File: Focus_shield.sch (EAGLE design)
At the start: 61 parts, among them U1 ARDUINO_SHIELDNOHOLES

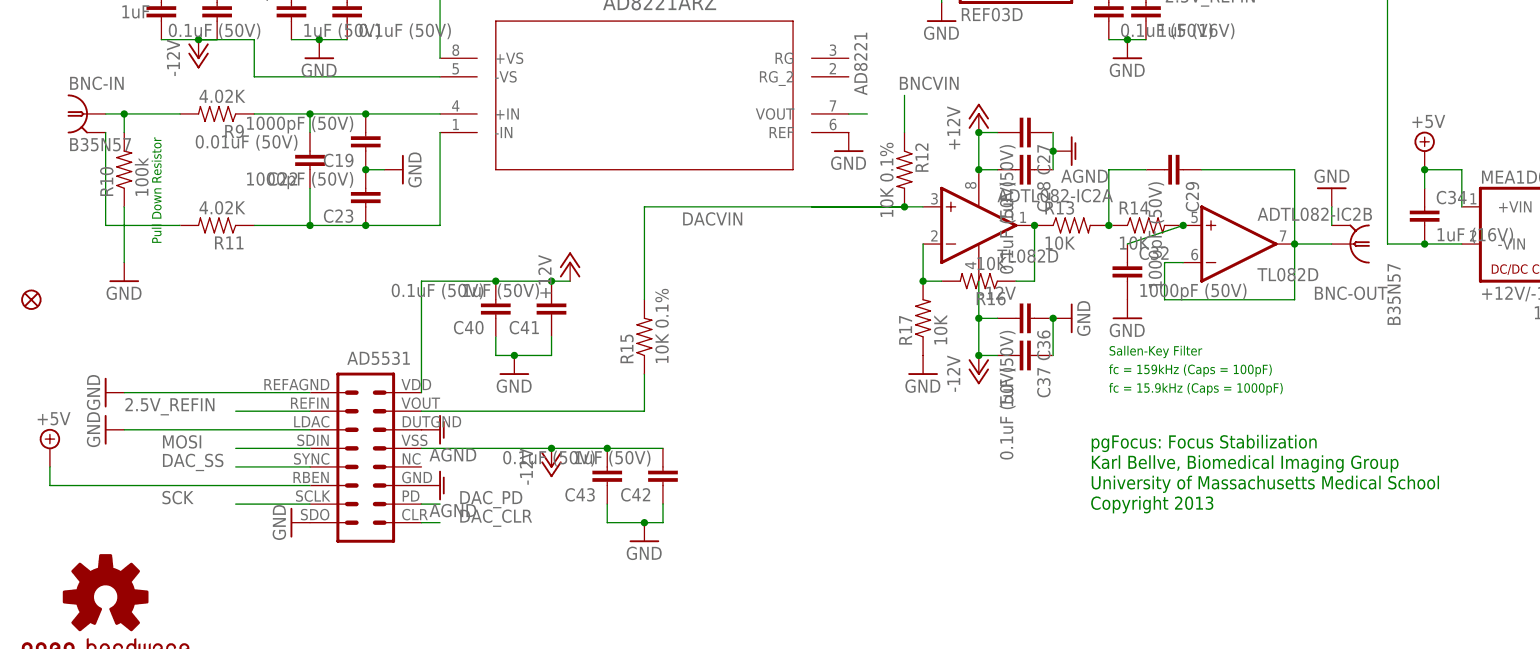
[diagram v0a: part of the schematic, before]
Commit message: switch type of BNC users, and added a link to BOM spreadsheet
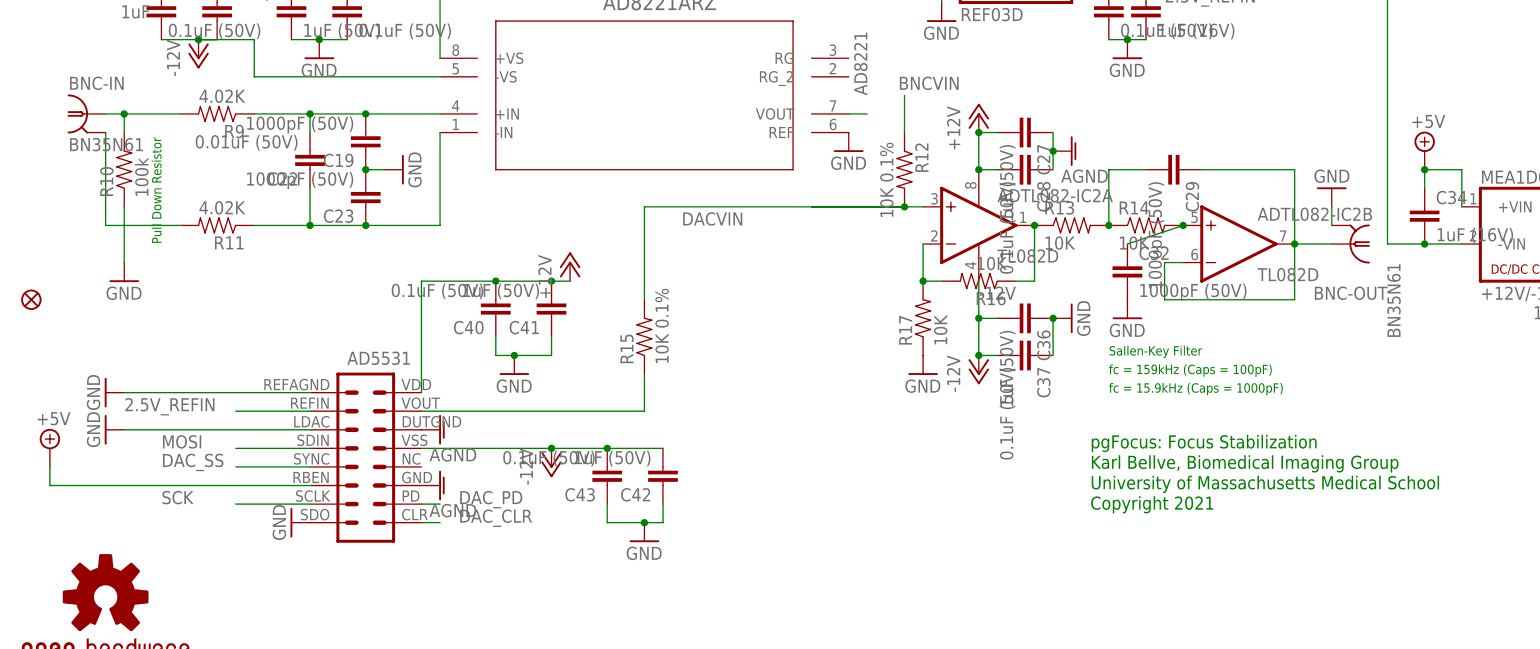
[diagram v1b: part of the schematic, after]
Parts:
- BNC-IN, BNC-OUT: value B35N57 -> BN35N61; device con-coax:B35N57 -> con-coax:BN35N61
- renumbered U$1 to AD5331
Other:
- note added: "Copyright 2021"
- note removed: "Copyright 2013"
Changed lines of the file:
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@@
 <part name="GND16" library="SparkFun-Aesthetics" deviceset="GND" device=""/>
 <part name="GND18" library="SparkFun" deviceset="GND" device=""/>
-<part name="U$1" library="BIG" deviceset="AD5331" device="" value="AD5531"/>
+<part name="AD5331" library="BIG" deviceset="AD5331" device="" value="AD5531"/>
 <part name="GND50" library="supply1" deviceset="AGND" device=""/>
 <part name="GND33" library="SparkFun" deviceset="GND" device=""/>
@@
 <part name="SUPPLY14" library="supply2" deviceset="+5V" device=""/>
 <part name="GND2" library="SparkFun" deviceset="GND" device=""/>
-<part name="BNC-OUT" library="con-coax" deviceset="B35N57" device=""/>
-<part name="BNC-IN" library="con-coax" deviceset="B35N57" device=""/>
+<part name="BNC-OUT" library="con-coax" library_urn="urn:adsk.eagle:library:133" deviceset="BN35N61" device="" package3d_urn="urn:adsk.eagle:package:6201/1"/>
+<part name="BNC-IN" library="con-coax" library_urn="urn:adsk.eagle:library:133" deviceset="BN35N61" device="" package3d_urn="urn:adsk.eagle:package:6201/1"/>
 <part name="GND3" library="SparkFun" deviceset="GND" device=""/>
 <part name="GND6" library="SparkFun-Aesthetics" deviceset="GND" device=""/>
@@
 <text x="91.44" y="35.306" size="1.778" layer="91">Karl Bellve, Biomedical Imaging Group</text>
 <text x="91.44" y="32.512" size="1.778" layer="91">University of Massachusetts Medical School</text>
-<text x="91.44" y="29.718" size="1.778" layer="91">Copyright 2013</text>
+<text x="91.44" y="29.718" size="1.778" layer="91">Copyright 2021</text>
 <text x="12.7" y="160.02" size="1.778" layer="91">AD7894-10</text>
 <text x="-17.78" y="154.94" size="1.778" layer="91">5kHz RC Low-pass</text>
@@
 <attribute name="VALUE" x="-33.02" y="127" size="1.778" layer="96"/>
 </instance>
-<instance part="U$1" gate="G$1" x="-7.62" y="35.56" smashed="yes"/>
+<instance part="AD5331" gate="G$1" x="-7.62" y="35.56" smashed="yes"/>
 <instance part="GND50" gate="VR1" x="2.54" y="40.64" smashed="yes" rot="R90">
 <attribute name="VALUE" x="7.62" y="38.1" size="1.778" layer="96" rot="R180"/>
@@
 </segment>
 <segment>
-<pinref part="U$1" gate="G$1" pin="LDAC"/>
+<pinref part="AD5331" gate="G$1" pin="LDAC"/>
 <pinref part="GND28" gate="1" pin="GND"/>
 <wire x1="-40.64" y1="40.64" x2="-15.24" y2="40.64" width="0.1524" layer="91"/>
 </segment>
 <segment>
-<pinref part="U$1" gate="G$1" pin="REFAGND"/>
+<pinref part="AD5331" gate="G$1" pin="REFAGND"/>
 <pinref part="GND33" gate="1" pin="GND"/>
 <wire x1="-40.64" y1="45.72" x2="-15.24" y2="45.72" width="0.1524" layer="91"/>
@@
 </segment>
 <segment>
-<pinref part="U$1" gate="G$1" pin="GND"/>
+<pinref part="AD5331" gate="G$1" pin="GND"/>
 <pinref part="GND14" gate="VR1" pin="AGND"/>
 </segment>
 <segment>
-<pinref part="U$1" gate="G$1" pin="DUTGND"/>
+<pinref part="AD5331" gate="G$1" pin="DUTGND"/>
 <pinref part="GND50" gate="VR1" pin="AGND"/>
 </segment>
 <segment>
-<pinref part="U$1" gate="G$1" pin="SDO"/>
+<pinref part="AD5331" gate="G$1" pin="SDO"/>
 <pinref part="GND20" gate="1" pin="GND"/>
 </segment>
@@
 <junction x="17.78" y="38.1"/>
 <wire x1="17.78" y1="38.1" x2="0" y2="38.1" width="0.1524" layer="91"/>
-<pinref part="U$1" gate="G$1" pin="VSS"/>
+<pinref part="AD5331" gate="G$1" pin="VSS"/>
 </segment>
 <segment>
@@
 <wire x1="-15.24" y1="30.48" x2="-25.4" y2="30.48" width="0.1524" layer="91"/>
 <label x="-35.56" y="30.48" size="1.778" layer="95"/>
-<pinref part="U$1" gate="G$1" pin="SCLK"/>
+<pinref part="AD5331" gate="G$1" pin="SCLK"/>
 </segment>
 <segment>
@@
 <wire x1="30.48" y1="43.18" x2="0" y2="43.18" width="0.1524" layer="91"/>
 <pinref part="R15" gate="G$1" pin="1"/>
-<pinref part="U$1" gate="G$1" pin="VOUT"/>
+<pinref part="AD5331" gate="G$1" pin="VOUT"/>
 </segment>
 </net>
@@
 </segment>
 <segment>
-<pinref part="U$1" gate="G$1" pin="RBEN"/>
+<pinref part="AD5331" gate="G$1" pin="RBEN"/>
 <pinref part="SUPPLY21" gate="+5V" pin="+5V"/>
 <wire x1="-15.24" y1="33.02" x2="-50.8" y2="33.02" width="0.1524" layer="91"/>
@@
 <wire x1="-15.24" y1="43.18" x2="-25.4" y2="43.18" width="0.1524" layer="91"/>
 <label x="-40.64" y="43.18" size="1.778" layer="95"/>
-<pinref part="U$1" gate="G$1" pin="REFIN"/>
+<pinref part="AD5331" gate="G$1" pin="REFIN"/>
 </segment>
 <segment>
@@
 <wire x1="-15.24" y1="35.56" x2="-25.4" y2="35.56" width="0.1524" layer="91"/>
 <label x="-35.56" y="35.56" size="1.778" layer="95"/>
-<pinref part="U$1" gate="G$1" pin="SYNC"/>
+<pinref part="AD5331" gate="G$1" pin="SYNC"/>
 </segment>
 <segment>
@@
 <wire x1="-15.24" y1="38.1" x2="-25.4" y2="38.1" width="0.1524" layer="91"/>
 <label x="-35.56" y="38.1" size="1.778" layer="95"/>
-<pinref part="U$1" gate="G$1" pin="SDIN"/>
+<pinref part="AD5331" gate="G$1" pin="SDIN"/>
 </segment>
 <segment>
@@
 <wire x1="0" y1="27.94" x2="2.54" y2="27.94" width="0.1524" layer="91"/>
 <label x="5.08" y="27.94" size="1.778" layer="95"/>
-<pinref part="U$1" gate="G$1" pin="CLR"/>
+<pinref part="AD5331" gate="G$1" pin="CLR"/>
 </segment>
 <segment>
@@
 <wire x1="0" y1="30.48" x2="2.54" y2="30.48" width="0.1524" layer="91"/>
 <label x="5.08" y="30.48" size="1.778" layer="95"/>
-<pinref part="U$1" gate="G$1" pin="PD"/>
+<pinref part="AD5331" gate="G$1" pin="PD"/>
 </segment>
 <segment>
@@
 <pinref part="C40" gate="G$1" pin="2"/>
 <wire x1="0" y1="60.96" x2="0" y2="45.72" width="0.1524" layer="91"/>
-<pinref part="U$1" gate="G$1" pin="VDD"/>
+<pinref part="AD5331" gate="G$1" pin="VDD"/>
 <wire x1="10.16" y1="60.96" x2="0" y2="60.96" width="0.1524" layer="91"/>
 <junction x="10.16" y="60.96"/>
@@
 </schematic>
 </drawing>
+<compatibility>
+<note version="8.2" severity="warning">
+Since Version 8.2, EAGLE supports online libraries. The ids
+of those online libraries will not be understood (or retained)
+with this version.
+</note>
+<note version="8.3" severity="warning">
+Since Version 8.3, EAGLE supports URNs for individual library
+assets (packages, symbols, and devices). The URNs of those assets
+will not be understood (or retained) with this version.
+</note>
+<note version="8.3" severity="warning">
+Since Version 8.3, EAGLE supports the association of 3D packages
+with devices in libraries, schematics, and board files. Those 3D
+packages will not be understood (or retained) with this version.
+</note>
+</compatibility>
 </eagle>

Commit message: moved +-12V DC power supply to other side of board to prevent shorting on Arduion USB connector. Still working on the design...not validated yet!
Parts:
- removed L3: 47uH, BIG:11R473C
- added L1, L2: 47uH, BIG:11R473C
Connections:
- new net N$8: L1.2, MEA1D0512SC.-VOUT
- net +12V: now also L2.2; no longer L3.2
- net +5V: no longer ICSP.VCC
- net -12V: now also L1.1; no longer MEA1D0512SC.-VOUT
- net N$6: now also L2.1; no longer L3.1
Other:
- moved on the sheet: C20, C21, C24, C25, C34, C38, C39, MEA1D0512SC

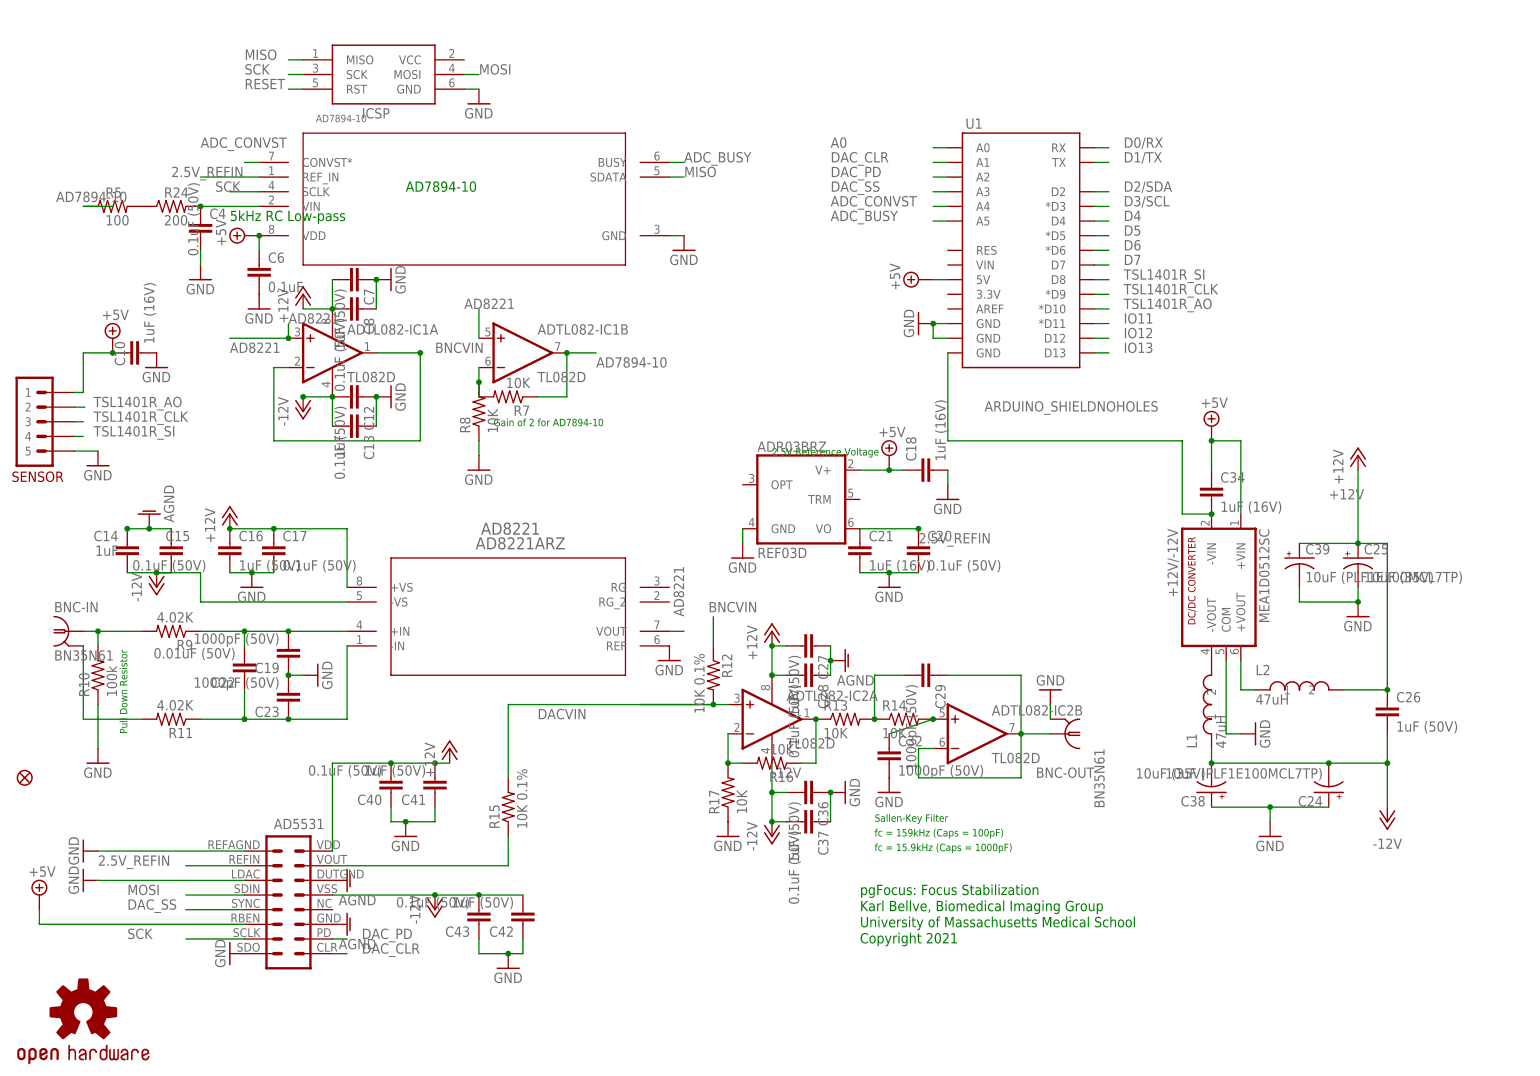
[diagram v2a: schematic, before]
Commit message: Reworked traces. Moved power lines to the bottom. Not validated yet!
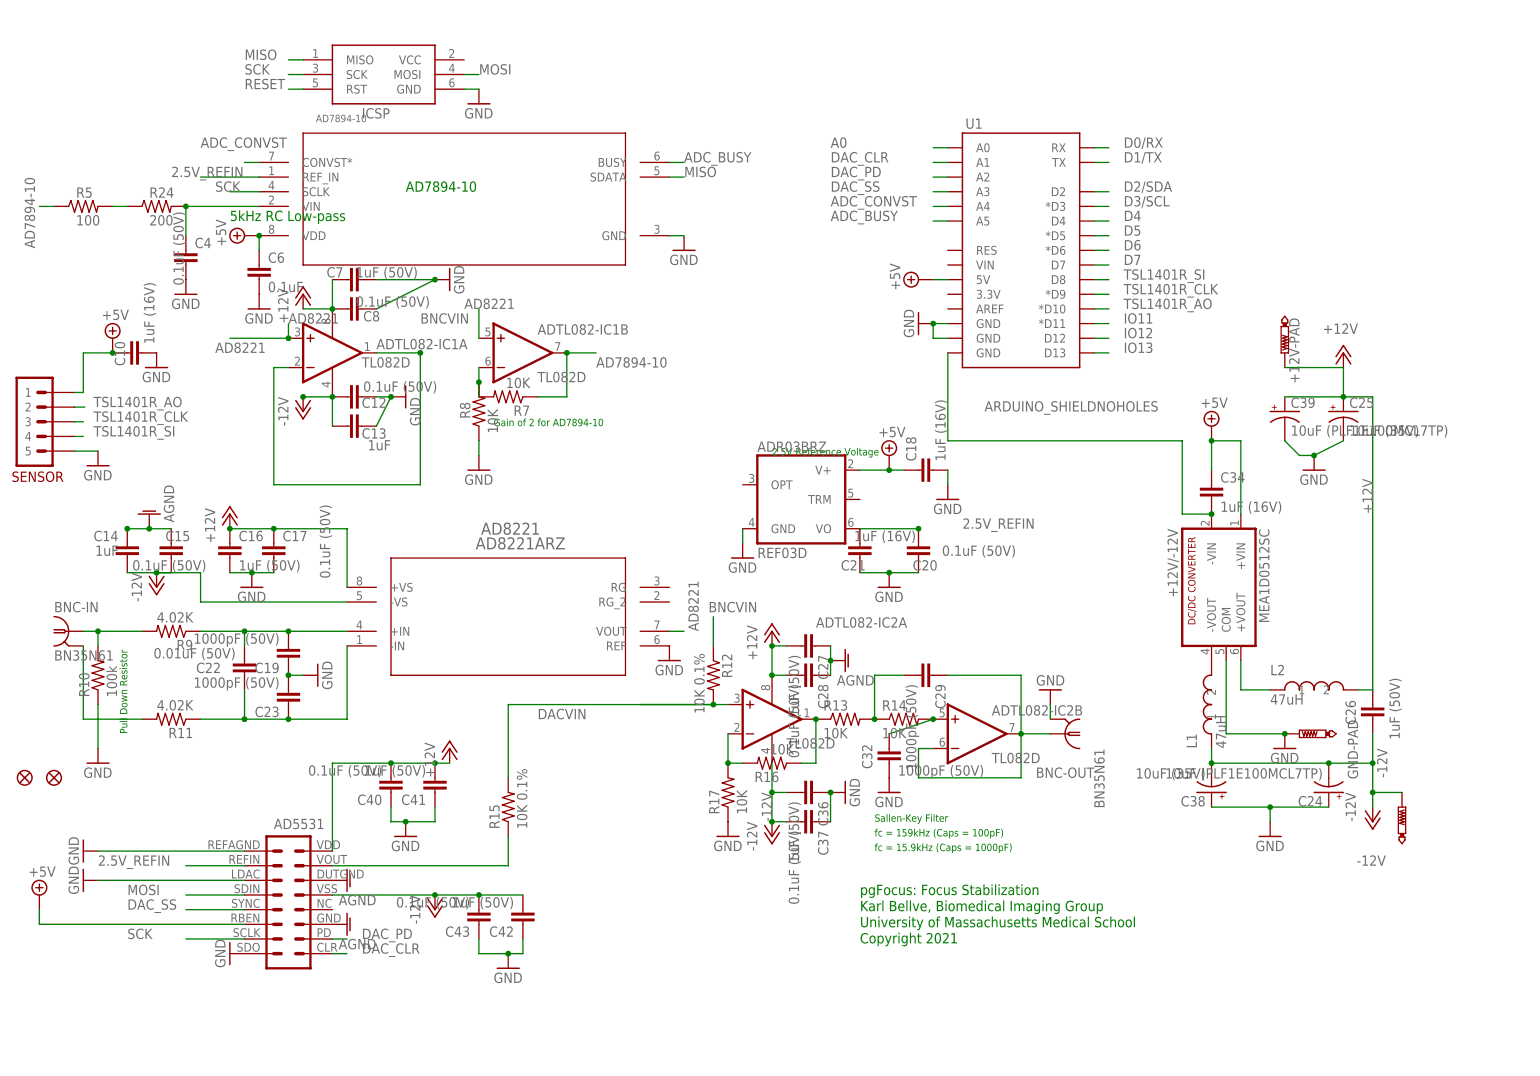
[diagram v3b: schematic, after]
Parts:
- removed U$3: OSHW-LOGOL, SparkFun:OSHW-LOGOL
- added +12V-PAD, -12V, GND-PAD: PTR1TP20R, testpad:PTR1TP20R
- added JP2: FIDUCIAL1.5X3, SparkFun:FIDUCIAL1.5X3
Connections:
- net +12V: now also +12V-PAD.TP
- net -12V: now also -12V.TP
- net GND: now also GND-PAD.TP
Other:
- moved on the sheet: C25, C26, C39, C4, L2, R24, R5

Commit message: Added solder jumnpers to adjust voltage range and gain settings of the ADC and DAC chips. Still untested!
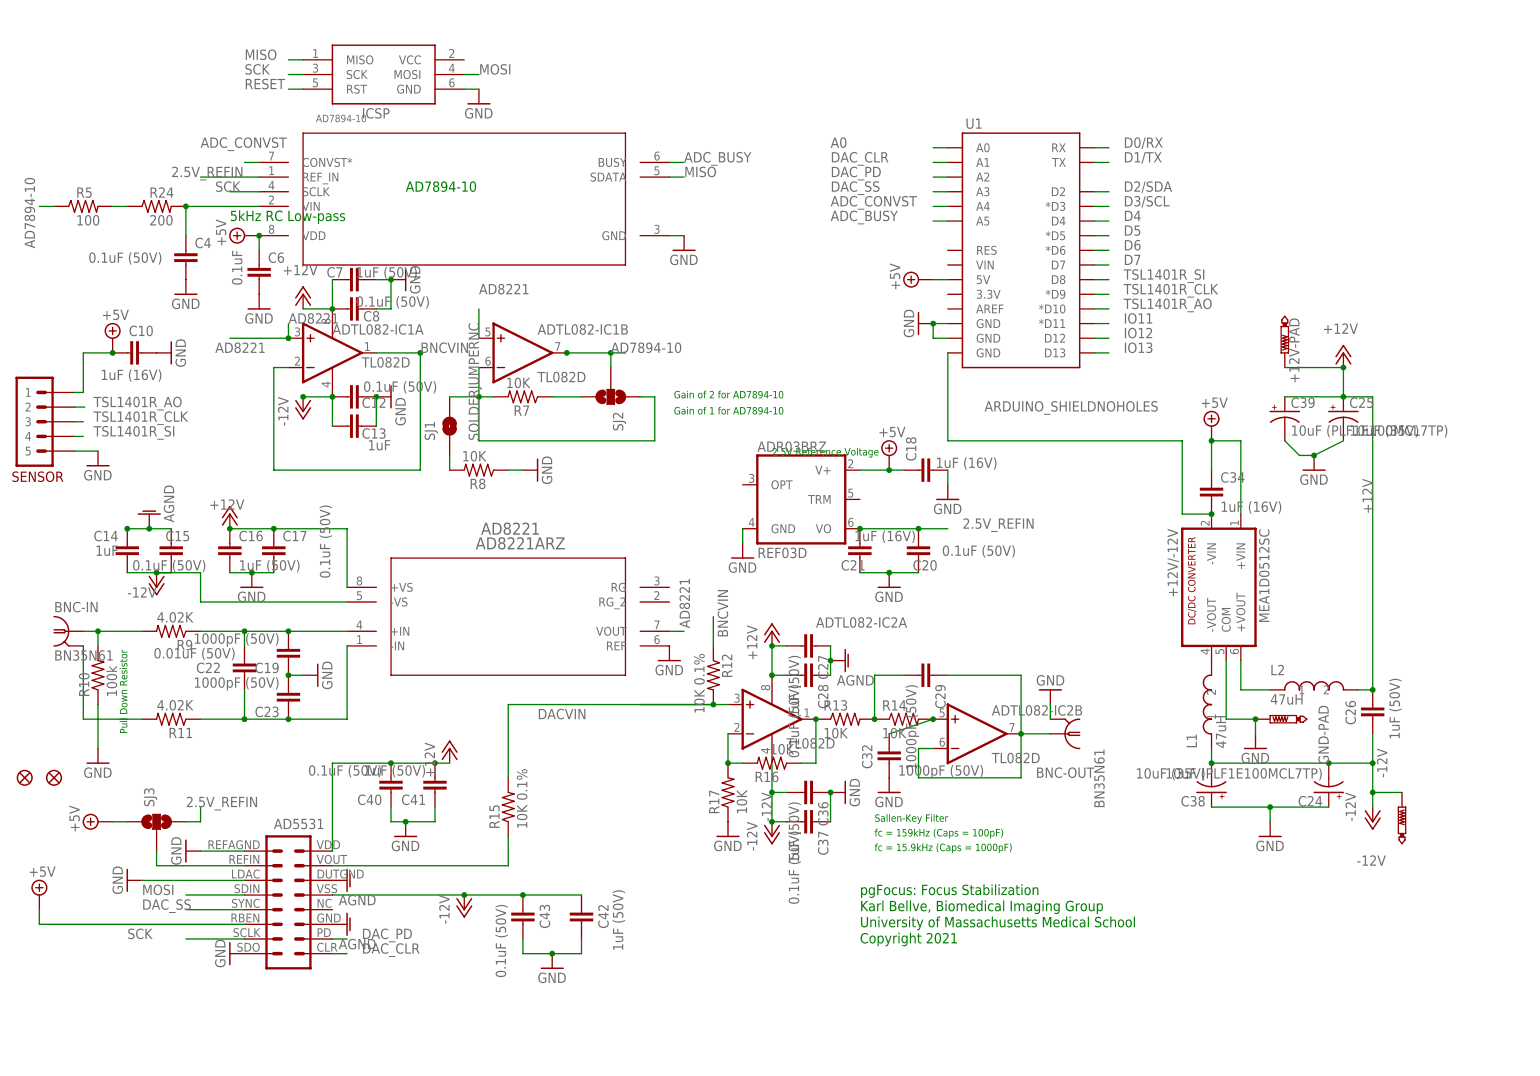
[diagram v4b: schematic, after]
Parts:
- added SJ1: SOLDERJUMPERNC, SparkFun-Passives:SOLDERJUMPERNC
- added SJ2, SJ3: (no value), SparkFun-Passives:SOLDERJUMPER_2WAYPASTE2&3
- AD5331: value AD5531 -> AD5331
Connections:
- new net N$10: R8.2, SJ1.1
- new net N$9: R7.1, SJ2.3
- new net REFIN: AD5331.REFIN, SJ3.2
- net +5V: now also SJ3.1
- net 2.5V_REFIN: now also SJ3.3; no longer AD5331.REFIN
- net AD7894-10: now also SJ2.2; no longer R7.1
- net N$18: now also SJ1.2, SJ2.1; no longer R8.2
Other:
- note added: "Gain of 1 for AD7894-10"
- moved on the sheet: C42, C43, GND-PAD, R7, R8
